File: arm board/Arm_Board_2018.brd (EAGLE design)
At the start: 236.5 x 96.8 mm, 208 parts, among them J1 RJ45KEYSTONE-942, J10 APP_2POS_CONFIGGENERAL_CONFIG, J11 APP_2POS_CONFIGGENERAL_CONFIG, J12 APP_2POS_CONFIGGENERAL_CONFIG, J13 APP_2POS_CONFIGGENERAL_CONFIG, J14 SL02, J15 SL02, J16 SL02, J2 JTAG_ARM_10PIN, J4 SL02, J5 APP_2POS_CONFIGGENERAL_CONFIG, J6 APP_2POS_CONFIGGENERAL_CONFIG, J7 APP_2POS_CONFIGGENERAL_CONFIG, J9 APP_2POS_CONFIGGENERAL_CONFIG, Q1 Q_IRF7437SMD, U1 TM4C1294NCPDT, U2 HX1198FNL, U3 SLVU2.8-4, Y1 NX3225GA, Y2 CRYATL_32K_SMD

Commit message: Made schematic changes from CDR
Still need to finish the board but the schematic was finished with the
exception of some pin allocations
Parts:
- moved C54 402.0 mm to (135.6, 69.1), turned to 180 degrees
- moved U$28 401.8 mm to (135.6, 66.5), turned to 180 degrees
- moved R54 392.1 mm to (126.2, 88.4)
- moved R55 391.8 mm to (126.2, 87.1)
- moved C50 379.7 mm to (30.5, 4.32), turned to 180 degrees
- moved J16 355.8 mm to (105.7, 80.3), turned to 180 degrees
- moved J15 352.5 mm to (105.7, 86.4), turned to 180 degrees
- moved J14 349.4 mm to (105.7, 92.2), turned to 180 degrees
- moved R51 279.3 mm to (101.3, 89.9), turned to 90 degrees
- moved R52 276.9 mm to (101.3, 84.6), turned to 90 degrees
- moved R58 276.7 mm to (73.9, 13.5), turned to 180 degrees
- moved U$10 275.4 mm to (78.2, 80.0), turned to 180 degrees
- moved R53 274.2 mm to (101.6, 79.8), turned to 90 degrees
- moved J4 272.0 mm to (6.35, 72.4), turned to 90 degrees
- moved C53 265.5 mm to (39.9, 9.65)
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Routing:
- net LOGIC_3.3V: track 90.4 -> 529.8 mm, vias 1 -> 13
- net 12VMOTOR_POWER: track 50.2 -> 275.6 mm, vias 19 -> 30
- net MOTOR3_DEMUX_SEL: track 0.00 -> 145.5 mm, vias 0 -> 4
- net MOTOR4_NFAULT: track 8.30 -> 143.3 mm, vias 0 -> 2
- net MOTOR4_NRESET: track 6.32 -> 137.4 mm, vias 0 -> 4
- net MOTOR8_NFAULT: track 8.06 -> 138.6 mm, vias 0 -> 2
- net MOTOR4_POWER: track 31.8 -> 161.2 mm, vias 1 -> 2
- net MOTOR8_NRESET: track 9.73 -> 135.1 mm, vias 0 -> 3
- net MOTOR8_PHASE: track 4.10 -> 129.4 mm, vias 0 -> 4
- net MOTOR5_PHASE: track 5.19 -> 129.7 mm, vias 0 -> 2
- net MOTOR3_GEN1: track 0.00 -> 124.2 mm, vias 0 -> 3
- net MOTOR5_NRESET: track 7.57 -> 128.5 mm, vias 0 -> 2
- net MOTOR5_NFAULT: track 9.62 -> 130.3 mm, vias 0 -> 2
- net MOTOR7_PHASE: track 1.98 -> 121.7 mm, vias 0 -> 2
- net LED5: track 0.00 -> 119.3 mm, vias 0 -> 2
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- added copper zone on layer 15, net GND
- added copper zone on layer 1, net MOTOR6_POWER
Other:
- board size 236.5 x 96.8 mm -> 193.6 x 118.1 mm
- board text added: "Missouri S&T Mars Rover Design Team Arm Board 2017 | Rev 1 David Strickland"
- board text removed: "Missouri S&T Mars Rover Design Team BOARD NAME 2017 | Rev 1 David Strickland"

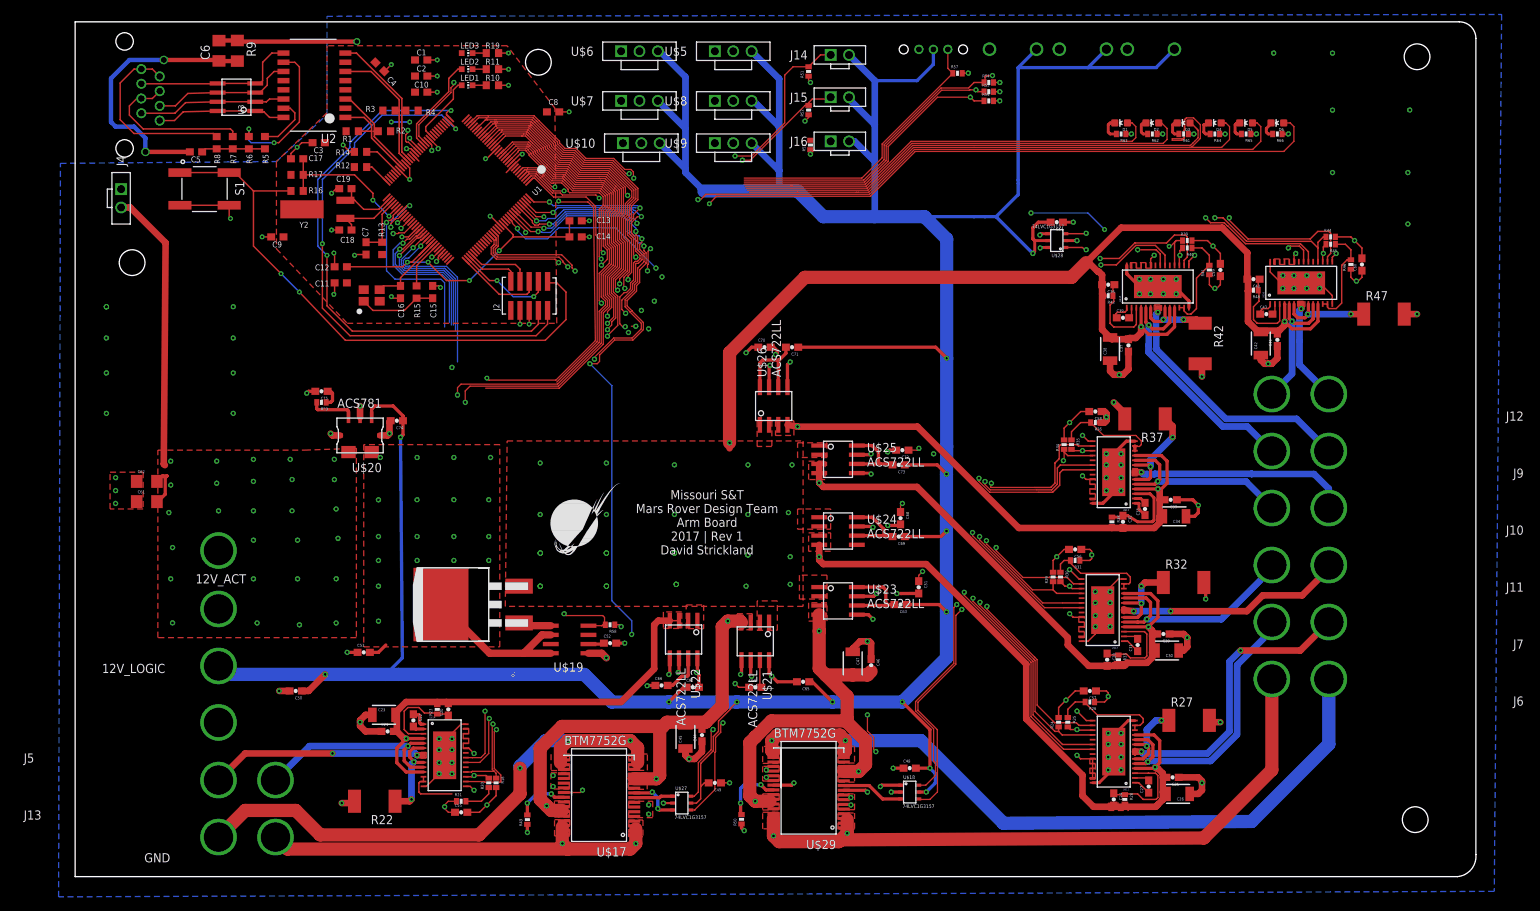
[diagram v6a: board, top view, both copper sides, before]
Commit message: Add all pins, finished Rev 1, Not board reviewed
Added all the pins that were missing. Finished routing all logic lines.
Made board slightly smaller.
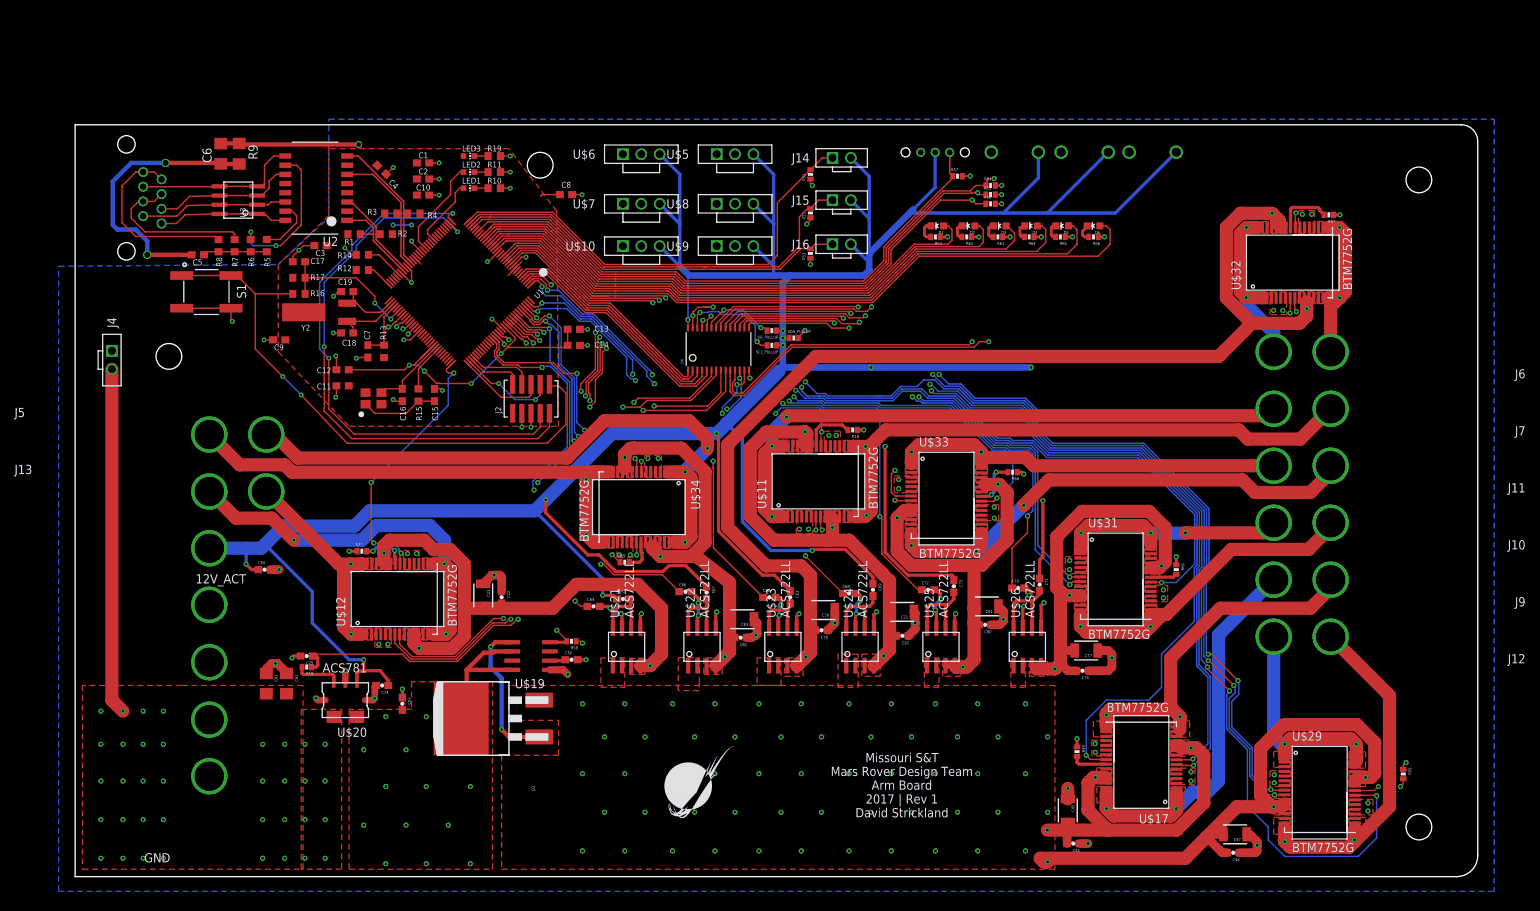
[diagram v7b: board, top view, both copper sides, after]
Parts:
- removed C24, C25, C28, C29, C32, C33, C36, C37, C40, C41, C48, C49, C54: .1uF, SparkFun-Passives:0603-CAP
- removed C26, C30, C34, C38, C42: 100uF, SparkFun-Passives:1210
- removed C27, C31, C35, C39, C43: .01uF, SparkFun-Passives:0603-CAP
- removed C55, C56, C57, C58, C59, C60: .47uF, SparkFun-Passives:0603-CAP
- removed R21, R24, R26, R29, R31, R34, R36, R39, R41, R44, R46: 10K, SparkFun-Passives:0402-RES
- removed R22, R27, R32, R37, R42, R47: 40m, SparkFun-Passives:R2512
- removed R23, R28, R33, R38, R43, R48: 1m, SparkFun-Passives:0402-RES
- removed R25, R30, R35, R40, R45: 22.6K, SparkFun-Passives:0402-RES
- removed U$13, U$14, U$15, U$16: DRV8829, MRDT-ICs:TSSOP28-GROUNDPAD
- removed U$18, U$27, U$28: 74LVC1G3157, MRDT-ICs:TSSOP-6
- added C76, C78, C80, C82: .1uF, SparkFun-Passives:0603-CAP
- added C77, C79, C81, C83: 100uF, SparkFun-Passives:1210
- added GROUND: APPPP45_PCB_HORIZ_RIGHT, MRDT-Connectors:APP45_PCB_HORIZ_RIGHT
- added OE_PULLUP, R60, R67, R68, R69: 10K, SparkFun-Passives:0402-RES
- added SCL_PULLUP, SDA_PULLUP: 1K, SparkFun-Passives:0402-RES
- added U$31, U$32, U$33, U$34: BTM7752G, MRDT-ICs:36-BSSOP
- added U4: (no value), adafruit:TSSOP28
- C21: value .1uF -> 100uF; device SparkFun-Passives:0603-CAP -> SparkFun-Passives:1210
- C22: value .01uF -> .1uF
- D1: value (none) -> J1
- D2: value (none) -> J2
- D3: value (none) -> J3
- D4: value (none) -> J4
- D5: value (none) -> J5
- D6: value (none) -> J6
- R20: value 22.6K -> 10K
- U$11, U$12: value DRV8829 -> BTM7752G; device MRDT-ICs:TSSOP28-GROUNDPAD -> MRDT-ICs:36-BSSOP
- moved U$12 92.0 mm to (50.0, 17.0), turned to 90 degrees
- moved R50 91.7 mm to (183.5, -7.16), turned to 270 degrees
- moved R49 76.5 mm to (138.4, -4.06), turned to 270 degrees
- moved U$17 75.1 mm to (147.3, 0.00)
- moved C21 73.0 mm to (114.3, 15.2), turned to 180 degrees
- moved U$29 71.6 mm to (172.0, -15.2), turned to 0 degrees
- moved R18 69.3 mm to (107.4, 40.4), turned to 180 degrees
- moved C20 63.6 mm to (114.3, 11.9), turned to 180 degrees
- moved C47 57.9 mm to (160.3, -15.5), turned to 180 degrees
- moved C46 56.3 mm to (160.0, -18.0), turned to 180 degrees
- moved C45 53.8 mm to (137.2, -12.2), turned to 270 degrees
- moved C44 53.5 mm to (137.9, -16.8), turned to 180 degrees
- moved U$11 51.4 mm to (108.2, 33.3), turned to 90 degrees
- moved U$26 48.3 mm to (131.6, 10.4)
- moved C70 48.3 mm to (130.3, 18.5)
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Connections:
- removed net MOTOR1_DEMUX_SEL: U$27.4, U1.P$4
- removed net MOTOR1_GEN0: U$27.6, U1.P$43
- removed net MOTOR2_GEN1: U$14.21, U1.P$44
- removed net MOTOR2_NFAULT: R18.1, U$14.18, U1.P$15
- removed net MOTOR2_NRESET: U$14.16, U1.P$14
- removed net MOTOR2_PHASE: U$14.20, U1.P$13
- removed net MOTOR3_DEMUX_SEL: U$18.4, U1.P$126
- removed net MOTOR3_GEN1: U$18.6, U1.P$45
- removed net MOTOR4_GEN2: U$11.21, U1.P$49
- removed net MOTOR4_NFAULT: R24.1, U$11.18, U1.P$12
- removed net MOTOR4_NRESET: U$11.16, U1.P$123
- removed net MOTOR4_PHASE: U$11.20, U1.P$124
- removed net MOTOR5_GEN2: U$12.21, U1.P$50
- removed net MOTOR5_NFAULT: R29.1, U$12.18, U1.P$25
- removed net MOTOR5_NRESET: U$12.16, U1.P$24
- removed net MOTOR5_PHASE: U$12.20, U1.P$23
- removed net MOTOR6_GEN3: U$13.21, U1.P$63
- removed net MOTOR6_NFAULT: R34.1, U$13.18, U1.P$109
- removed net MOTOR6_NRESET: U$13.16, U1.P$110
- removed net MOTOR6_PHASE: U$13.20, U1.P$111
- removed net MOTOR7/8_DEMUX_SEL: U$28.4, U1.P$128
- removed net MOTOR7/8_GEN3: U$28.6, U1.P$62
- removed net MOTOR7_NFAULT: R39.1, U$15.18, U1.P$6
- removed net MOTOR7_NRESET: U$15.16, U1.P$11
- removed net MOTOR7_PHASE: U$15.20, U1.P$27
- removed net MOTOR7_PWM: U$15.21, U$28.1
- removed net MOTOR8_NFAULT: R44.1, U$16.18, U1.P$5
- removed net MOTOR8_NRESET: U$16.16, U1.P$118
- removed net MOTOR8_PHASE: U$16.20, U1.P$119
- removed net MOTOR8_PWM: U$16.21, U$28.3
- removed net N$1: C55.2, R18.2, R20.2, U$14.15, U$14.17, U$14.23, U$14.24, U$14.25, U$14.26, U$14.27
- removed net N$10: C22.1, U$14.1
- removed net N$11: C22.2, U$14.2
- removed net N$12: R20.1, R21.2, U$14.12, U$14.13
- removed net N$15: R35.1, R36.2, U$13.12, U$13.13
- removed net N$16: R27.1, U$11.6, U$11.9
- removed net N$17: C24.1, R28.1, U$11.3
- removed net N$18: C27.1, U$11.1
- removed net N$19: C27.2, U$11.2
- removed net N$20: C57.2, R24.2, R25.2, U$11.15, U$11.17, U$11.23, U$11.24, U$11.25, U$11.26, U$11.27
- removed net N$21: R45.1, R46.2, U$16.12, U$16.13
- removed net N$22: R32.1, U$12.6, U$12.9
- removed net N$23: C28.1, R33.1, U$12.3
- removed net N$24: C31.1, U$12.1
- removed net N$25: C31.2, U$12.2
- removed net N$27: R40.1, R41.2, U$15.12, U$15.13
- removed net N$28: R37.1, U$13.6, U$13.9
- removed net N$29: C32.1, R38.1, U$13.3
- removed net N$30: C35.1, U$13.1
- removed net N$31: C35.2, U$13.2
- removed net N$32: C59.2, R39.2, R40.2, U$15.15, U$15.17, U$15.23, U$15.24, U$15.25, U$15.26, U$15.27
- removed net N$33: C60.2, R44.2, R45.2, U$16.15, U$16.17, U$16.23, U$16.24, U$16.25, U$16.26, U$16.27
- removed net N$34: R42.1, U$15.6, U$15.9
- removed net N$35: C36.1, R43.1, U$15.3
- removed net N$36: C39.1, U$15.1
- removed net N$37: C39.2, U$15.2
- removed net N$38: C56.2, R29.2, R30.2, U$12.15, U$12.17, U$12.23, U$12.24, U$12.25, U$12.26, U$12.27
- removed net N$39: C58.2, R34.2, R35.2, U$13.15, U$13.17, U$13.23, U$13.24, U$13.25, U$13.26, U$13.27
- removed net N$40: R47.1, U$16.6, U$16.9
- removed net N$41: C40.1, R48.1, U$16.3
- removed net N$42: C43.1, U$16.1
- removed net N$43: C43.2, U$16.2
- removed net N$7: R22.1, U$14.6, U$14.9
- removed net N$8: C20.1, R23.1, U$14.3
- new net MOTOR2_ENABLE: U$34.27, U1.P$110
- new net MOTOR2_PWM1: U$34.9, U4.8
- new net MOTOR2_PWM2: U$34.10, U4.9
- new net MOTOR4_ENABLE: U$11.27, U1.P$116
- new net MOTOR4_PWM1: U$11.9, U4.12
- new net MOTOR4_PWM2: U$11.10, U4.13
- new net MOTOR5_ENABLE: U$33.27, U1.P$117
- new net MOTOR5_PWM1: U$33.9, U4.15
- new net MOTOR5_PWM2: U$33.10, U4.16
- new net MOTOR6_ENABLE: U$31.27, U1.P$118
- new net MOTOR6_PWM1: U$31.9, U4.17
- new net MOTOR6_PWM2: U$31.10, U4.18
- new net MOTOR7_ENABLE: U$17.27, U1.P$119
- new net MOTOR7_PWM1: U$17.9, U4.19
- new net MOTOR7_PWM2: U$17.10, U4.20
- new net MOTOR8_ENABLE: U$29.27, U1.P$120
- new net MOTOR8_PWM1: U$29.9, U4.21
- new net MOTOR8_PWM2: U$29.10, U4.22
- new net N$44: R60.2, U$31.28
- new net N$46: R67.2, U$32.28
- new net N$50: R68.2, U$33.28
- new net N$51: R69.2, U$34.28
- new net PWM_ADDRESS_BIT_A0: U1.P$12, U4.1
- new net PWM_ADDRESS_BIT_A1: U1.P$11, U4.2
- new net PWM_ADDRESS_BIT_A2: U1.P$6, U4.3
- new net PWM_ADDRESS_BIT_A3: U1.P$5, U4.4
- new net PWM_ADDRESS_BIT_A4: U1.P$4, U4.5
- new net PWM_ADDRESS_BIT_A5: U1.P$13, U4.24
- new net PWM_DRIVER_SCL: SCL_PULLUP.2, U1.P$112, U4.26
- new net PWM_DRIVER_SDA: SDA_PULLUP.2, U1.P$111, U4.27
- new net PWM_OUTPUT_ENABLE: OE_PULLUP.2, U1.P$14, U4.23
- net 12VMOTOR_POWER: now also C44.2, C45.2, C46.2, C47.2, U$17.11, U$17.12, U$17.13, U$17.14, U$17.29, U$17.30, U$17.31, U$17.32, U$29.11, U$29.12, U$29.13, U$29.14, U$29.29, U$29.30, U$29.31, U$29.32; no longer C36.2, C37.2, C38.2, C40.2, C41.2, C42.2, R43.2, R48.2, U$15.11, U$15.4, U$16.11, U$16.4
- net BUTTON1: now also U1.P$24; no longer U1.P$81
- net BUTTON2: now also U1.P$25; no longer U1.P$82
- net BUTTON3: now also U1.P$27; no longer U1.P$83
- net GND: now also C20.1, C22.1, C76.1, C77.1, C78.1, C79.1, C80.1, C81.1, C82.1, C83.1, GROUND.P$1, R18.1, R20.1, R60.1, R67.1, R68.1, R69.1, U$11.23, U$11.24, U$11.25, U$11.26, U$11.5, U$11.6, U$11.7, U$11.8, U$12.23, U$12.24, U$12.25, U$12.26, U$12.5, U$12.6, U$12.7, U$12.8, U$31.23, U$31.24, U$31.25, U$31.26, U$31.5, U$31.6, U$31.7, U$31.8, U$32.23, U$32.24, U$32.25, U$32.26, U$32.5, U$32.6, U$32.7, U$32.8, U$33.23, U$33.24, U$33.25, U$33.26, U$33.5, U$33.6, U$33.7, U$33.8, U$34.23, U$34.24, U$34.25, U$34.26, U$34.5, U$34.6, U$34.7, U$34.8, U4.14, U4.25; no longer C25.1, C26.1, C29.1, C30.1, C33.1, C34.1, C37.1, C38.1, C41.1, C42.1, C48.1, C49.1, C54.1, C55.1, C56.1, C57.1, C58.1, C59.1, C60.1, R21.1, R22.2, R26.1, R27.2, R31.1, R32.2, R36.1, R37.2, R41.1, R42.2, R46.1, R47.2, U$11.14, U$11.28, U$11.29, U$12.14, U$12.28, U$12.29, U$13.14, U$13.28, U$13.29, U$14.14, U$14.28, U$14.29, U$15.14, U$15.28, U$15.29, U$16.14, U$16.28, U$16.29, U$18.2, U$27.2, U$28.2
- net LED1: now also U1.P$23; no longer U1.P$37
- net LED2: now also U1.P$22; no longer U1.P$38
- net LED3: now also U1.P$21; no longer U1.P$91
- net LED4: now also U1.P$20; no longer U1.P$92
- net LED5: now also U1.P$19; no longer U1.P$22
- net LED6: now also U1.P$18; no longer U1.P$2
- net LIMIT_SWITCH_1: now also U1.P$32; no longer U1.P$29
- net LIMIT_SWITCH_2: now also U1.P$31; no longer U1.P$30
- net LIMIT_SWITCH_3: now also U1.P$30; no longer U1.P$61
- net LOGIC_3.3V: now also OE_PULLUP.1, SCL_PULLUP.1, SDA_PULLUP.1, U4.28; no longer C48.2, C49.2, C54.2, U$18.5, U$27.5, U$28.5
- net MAINLINE_CURRENT_SENSOR: now also U1.P$121; no longer U1.P$1
- net MASTER_POWER_ENABLE: now also U1.P$109; no longer U1.P$85
- net MOTOR1_1: now also U$12.1, U$12.2, U$12.3, U$12.33, U$12.34, U$12.35, U$12.36, U$12.4; no longer U$17.1, U$17.2, U$17.3, U$17.33, U$17.34, U$17.35, U$17.36, U$17.4
- net MOTOR1_2: now also U$12.15, U$12.16, U$12.17, U$12.18, U$12.19, U$12.20, U$12.21, U$12.22; no longer U$17.15, U$17.16, U$17.17, U$17.18, U$17.19, U$17.20, U$17.21, U$17.22
- net MOTOR1_CURRENT_SENSOR: now also U1.P$123; no longer U1.P$121
- net MOTOR1_ENABLE: now also U$12.27, U1.P$96; no longer U$17.27, U1.P$73
- net MOTOR1_POWER: now also C22.2, C23.2, U$12.11, U$12.12, U$12.13, U$12.14, U$12.29, U$12.30, U$12.31, U$12.32; no longer C44.2, C45.2, U$17.11, U$17.12, U$17.13, U$17.14, U$17.29, U$17.30, U$17.31, U$17.32
- net MOTOR1_PWM1: now also U$12.9, U4.6; no longer U$17.9, U$27.1
- net MOTOR1_PWM2: now also U$12.10, U4.7; no longer U$17.10, U$27.3
- net MOTOR2_1: now also U$34.1, U$34.2, U$34.3, U$34.33, U$34.34, U$34.35, U$34.36, U$34.4; no longer U$14.10, U$14.5
- net MOTOR2_2: now also U$34.15, U$34.16, U$34.17, U$34.18, U$34.19, U$34.20, U$34.21, U$34.22; no longer U$14.7, U$14.8
- net MOTOR2_CURRENT_SENSOR: now also U1.P$124; no longer U1.P$120
- net MOTOR2_POWER: now also C82.2, C83.2, U$34.11, U$34.12, U$34.13, U$34.14, U$34.29, U$34.30, U$34.31, U$34.32; no longer C20.2, C21.2, C23.2, R23.2, U$14.11, U$14.4
- net MOTOR3_1: now also U$32.1, U$32.2, U$32.3, U$32.33, U$32.34, U$32.35, U$32.36, U$32.4; no longer U$29.1, U$29.2, U$29.3, U$29.33, U$29.34, U$29.35, U$29.36, U$29.4
- net MOTOR3_2: now also U$32.15, U$32.16, U$32.17, U$32.18, U$32.19, U$32.20, U$32.21, U$32.22; no longer U$29.15, U$29.16, U$29.17, U$29.18, U$29.19, U$29.20, U$29.21, U$29.22
- net MOTOR3_CURRENT_SENSOR: now also U1.P$126; no longer U1.P$18
- net MOTOR3_ENABLE: now also U$32.27, U1.P$15; no longer U$29.27, U1.P$71
- net MOTOR3_POWER: now also C78.2, C79.2, U$32.11, U$32.12, U$32.13, U$32.14, U$32.29, U$32.30, U$32.31, U$32.32; no longer C46.2, C47.2, U$29.11, U$29.12, U$29.13, U$29.14, U$29.29, U$29.30, U$29.31, U$29.32
- net MOTOR3_PWM1: now also U$32.9, U4.10; no longer U$18.1, U$29.9
- net MOTOR3_PWM2: now also U$32.10, U4.11; no longer U$18.3, U$29.10
- net MOTOR4_1: now also U$11.1, U$11.2, U$11.3, U$11.33, U$11.34, U$11.35, U$11.36, U$11.4; no longer U$11.10, U$11.5
- net MOTOR4_2: now also U$11.15, U$11.16, U$11.17, U$11.18, U$11.19, U$11.20, U$11.21, U$11.22; no longer U$11.7, U$11.8
- net MOTOR4_CURRENT_SENSOR: now also U1.P$127; no longer U1.P$19
- net MOTOR4_POWER: now also C20.2, C21.2, U$11.12, U$11.13, U$11.14, U$11.29, U$11.30, U$11.31, U$11.32; no longer C24.2, C25.2, C26.2, R28.2, U$11.4
- net MOTOR5_1: now also U$33.1, U$33.2, U$33.3, U$33.33, U$33.34, U$33.35, U$33.36, U$33.4; no longer U$12.10, U$12.5
- net MOTOR5_2: now also U$33.15, U$33.16, U$33.17, U$33.18, U$33.19, U$33.20, U$33.21, U$33.22; no longer U$12.7, U$12.8
- net MOTOR5_CURRENT_SENSOR: now also U1.P$1; no longer U1.P$20
- net MOTOR5_POWER: now also C80.2, C81.2, U$33.11, U$33.12, U$33.13, U$33.14, U$33.29, U$33.30, U$33.31, U$33.32; no longer C28.2, C29.2, C30.2, R33.2, U$12.11, U$12.4
- net MOTOR6_1: now also U$31.1, U$31.2, U$31.3, U$31.33, U$31.34, U$31.35, U$31.36, U$31.4; no longer U$13.10, U$13.5
- net MOTOR6_2: now also U$31.15, U$31.16, U$31.17, U$31.18, U$31.19, U$31.20, U$31.21, U$31.22; no longer U$13.7, U$13.8
- net MOTOR6_CURRENT_SENSOR: now also U1.P$2; no longer U1.P$21
- net MOTOR6_POWER: now also C76.2, C77.2, U$31.11, U$31.12, U$31.13, U$31.14, U$31.29, U$31.30, U$31.31, U$31.32; no longer C32.2, C33.2, C34.2, R38.2, U$13.11, U$13.4
- net MOTOR7_1: now also U$17.1, U$17.2, U$17.3, U$17.33, U$17.34, U$17.35, U$17.36, U$17.4; no longer U$15.10, U$15.5
- net MOTOR7_2: now also U$17.15, U$17.16, U$17.17, U$17.18, U$17.19, U$17.20, U$17.21, U$17.22; no longer U$15.7, U$15.8
- net MOTOR8_1: now also U$29.1, U$29.2, U$29.3, U$29.33, U$29.34, U$29.35, U$29.36, U$29.4; no longer U$16.10, U$16.5
- net MOTOR8_2: now also U$29.15, U$29.16, U$29.17, U$29.18, U$29.19, U$29.20, U$29.21, U$29.22; no longer U$16.7, U$16.8
- net N$5: now also R18.2, U$11.28; no longer R30.1, R31.2, U$12.12, U$12.13
- net N$6: now also R20.2, U$12.28; no longer R25.1, R26.2, U$11.12, U$11.13
- net SWITCH: now also U1.P$29; no longer U1.P$84
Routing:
- net MOTOR3_POWER: track 104.1 -> 303.2 mm
- net MOTOR8_ENABLE: track 0.00 -> 187.6 mm, vias 0 -> 5
- net MOTOR3_2: track 195.7 -> 40.9 mm
- net MOTOR7_ENABLE: track 0.00 -> 154.1 mm, vias 0 -> 3
- net MOTOR3_DEMUX_SEL: track 145.5 -> 0.00 mm, vias 4 -> 0
- net MOTOR4_NFAULT: track 143.3 -> 0.00 mm, vias 2 -> 0
- net MOTOR8_NFAULT: track 138.6 -> 0.00 mm, vias 2 -> 0
- net MOTOR4_NRESET: track 137.4 -> 0.00 mm, vias 4 -> 0
- net MOTOR3_1: track 178.4 -> 42.6 mm
- net MOTOR8_NRESET: track 135.1 -> 0.00 mm, vias 3 -> 0
- net MOTOR5_NFAULT: track 130.3 -> 0.00 mm, vias 2 -> 0
- net MOTOR5_PHASE: track 129.7 -> 0.00 mm, vias 2 -> 0
- net MOTOR8_PHASE: track 129.4 -> 0.00 mm, vias 4 -> 0
- net MOTOR8_PWM2: track 0.00 -> 128.9 mm, vias 0 -> 5
- net MOTOR5_NRESET: track 128.5 -> 0.00 mm, vias 2 -> 0
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- added copper zone on layer 1, net MOTOR2_1
- added copper zone on layer 1, net MOTOR4_1
- added copper zone on layer 1, net MOTOR4_2
- added copper zone on layer 1, net MOTOR5_1
- added copper zone on layer 1, net MOTOR5_2
- added copper zone on layer 1, net MOTOR6_1
- added copper zone on layer 1, net MOTOR7_1
- added copper zone on layer 1, net MOTOR8_1
- removed copper zone on layer 1, net N$1
- removed copper zone on layer 1, net N$20
- removed copper zone on layer 1, net N$32
- removed copper zone on layer 1, net N$33
- removed copper zone on layer 1, net N$38
- removed copper zone on layer 1, net N$39
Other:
- board size 193.6 x 118.1 mm -> 193.8 x 103.9 mm
- board text removed: "12V_LOGIC"
